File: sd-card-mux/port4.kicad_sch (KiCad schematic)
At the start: 10 parts, among them J201 47309-2285, U201 74LVC1G3157, U202 74LVC1G3157, U203 74LVC1G3157, U204 74LVC1G3157, U205 74LVC1G3157, U206 74LVC1G3157

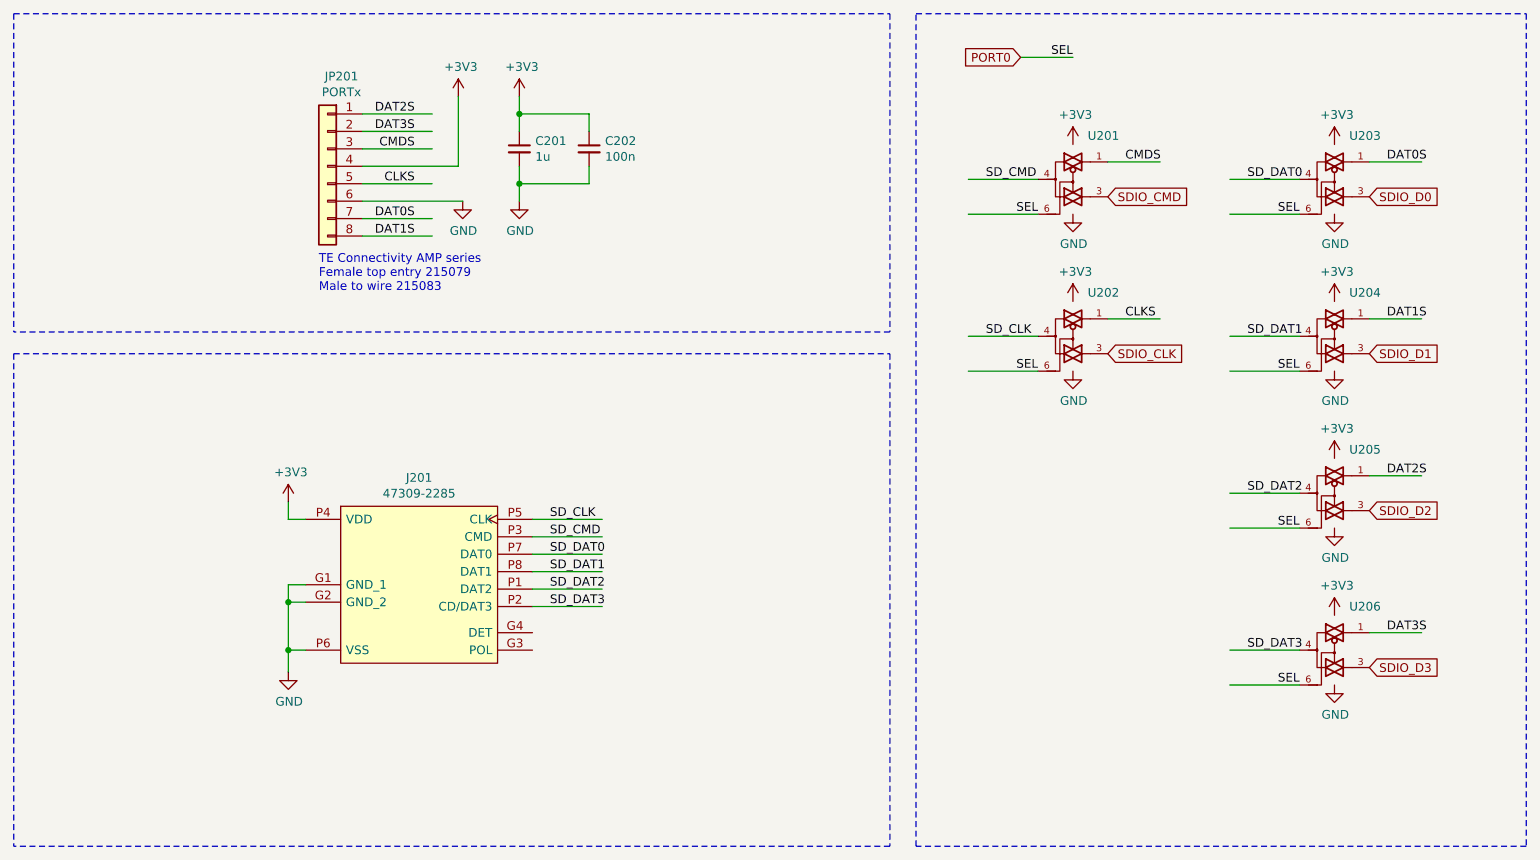
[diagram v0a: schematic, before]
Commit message: Added MCP23008 alternative
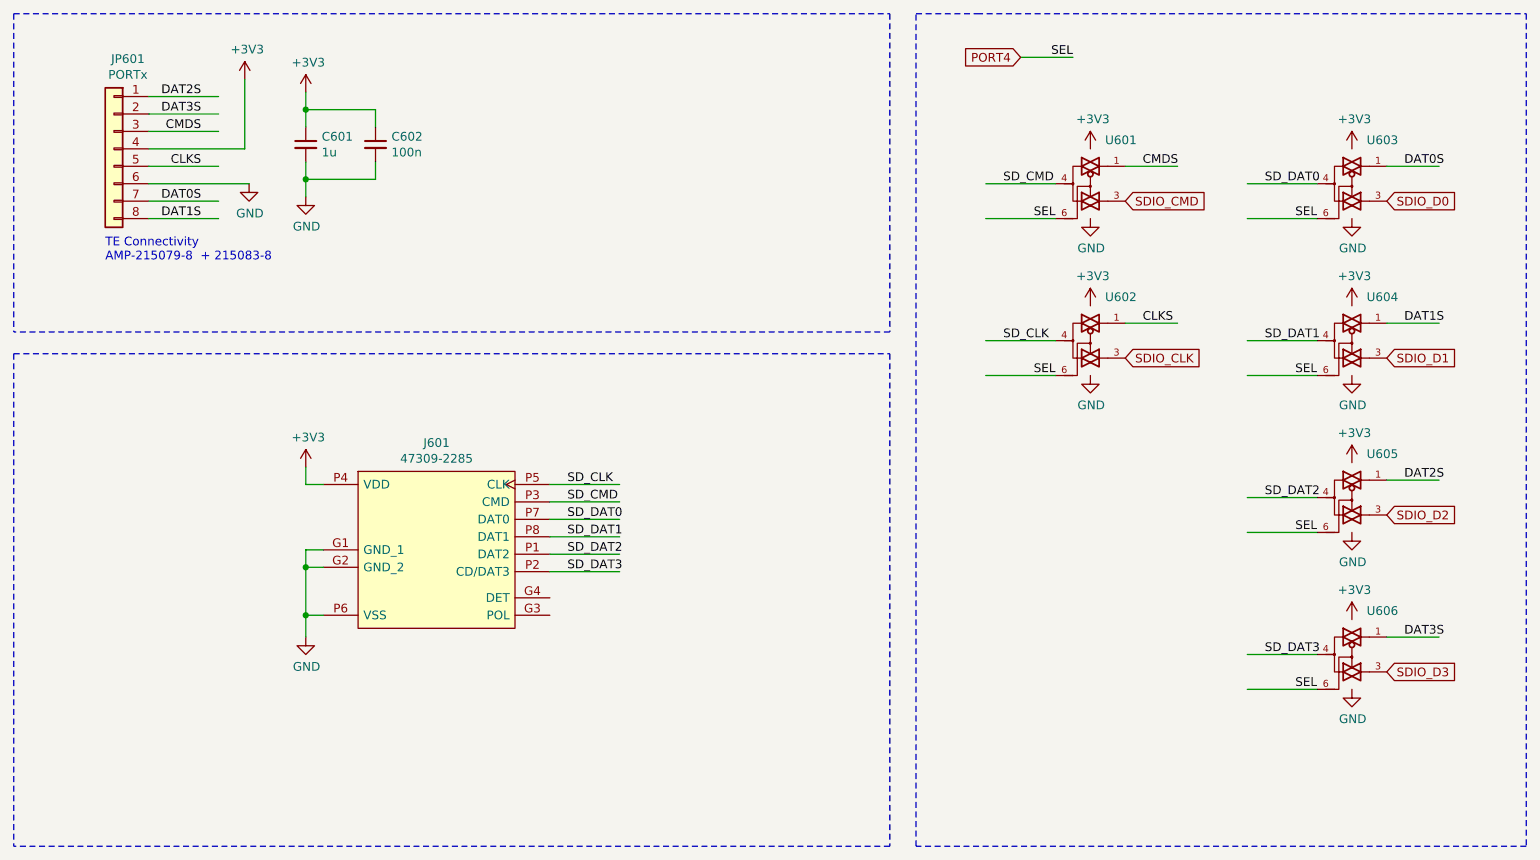
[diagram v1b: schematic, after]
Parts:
- removed C201: 1u, Capacitor_SMD:C_0402_1005Metric, symbol Device:C_Small
- removed C202: 100n, Capacitor_SMD:C_0402_1005Metric, symbol Device:C_Small
- removed J201: 47309-2285, footprints:47309-2285, symbol 47309-2285:47309-2285
- removed JP201: PORTx, Connector_JST:JST_PH_S8B-PH-K_1x08_P2.00mm_Horizontal, symbol Connector_Generic:Conn_01x08
- removed U201, U202, U203, U204, U205, U206: 74LVC1G3157, Package_TO_SOT_SMD:SOT-363_SC-70-6, symbol 74LVC1G3157:74LVC1G3157
- added C601: 1u, Capacitor_SMD:C_0402_1005Metric, symbol Device:C_Small
- added C602: 100n, Capacitor_SMD:C_0402_1005Metric, symbol Device:C_Small
- added J601: 47309-2285, footprints:47309-2285, symbol 47309-2285:47309-2285
- added JP601: PORTx, Connector_JST:JST_PH_S8B-PH-K_1x08_P2.00mm_Horizontal, symbol Connector_Generic:Conn_01x08
- added U601, U602, U603, U604, U605, U606: 74LVC1G3157, Package_TO_SOT_SMD:SOT-363_SC-70-6, symbol 74LVC1G3157:74LVC1G3157
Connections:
- net +3V3: now also C601.1, C602.1, J601.P4 (VDD), JP601.4 (Pin_4), U601.5 (VCC), U602.5 (VCC), U603.5 (VCC), U604.5 (VCC), U605.5 (VCC), U606.5 (VCC)
- net CLKS: now also JP601.5 (Pin_5), U602.1
- net CMDS: now also JP601.3 (Pin_3), U601.1
- net DAT0S: now also JP601.7 (Pin_7), U603.1
- net DAT1S: now also JP601.8 (Pin_8), U604.1
- net DAT2S: now also JP601.1 (Pin_1), U605.1
- net DAT3S: now also JP601.2 (Pin_2), U606.1
- net GND: now also C601.2, C602.2, J601.G1 (GND_1), J601.G2 (GND_2), J601.P6 (VSS), JP601.6 (Pin_6), U601.2 (GND), U602.2 (GND), U603.2 (GND), U604.2 (GND), U605.2 (GND), U606.2 (GND)
- net SDIO_CLK: now also U602.3
- net SDIO_CMD: now also U601.3
- net SDIO_D0: now also U603.3
- net SDIO_D1: now also U604.3
- net SDIO_D2: now also U605.3
- net SDIO_D3: now also U606.3
- net SD_CLK: now also J601.P5 (CLK), U602.4
- net SD_CMD: now also J601.P3 (CMD), U601.4
- net SD_DAT0: now also J601.P7 (DAT0), U603.4
- net SD_DAT1: now also J601.P8 (DAT1), U604.4
- net SD_DAT2: now also J601.P1 (DAT2), U605.4
- net SD_DAT3: now also J601.P2 (CD/DAT3), U606.4
- new net PORT4: U601.6, U602.6, U603.6, U604.6, U605.6, U606.6
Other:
- note added: "TE Connectivity AMP-215079-8 + 215083-8"
- note removed: "TE Connectivity AMP series Female top entry 215079 Male to wire 215083"

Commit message: Addedd missing upload port
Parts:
- C601: LCSC Part# (none) -> C52923
- C602: LCSC Part# (none) -> C1525
- JP601: footprint Connector_JST:JST_PH_S8B-PH-K_1x08_P2.00mm_Horizontal -> footprints:ConnectorMicromatch-8
- U601, U602, U603, U604, U605, U606: LCSC Part# (none) -> C38663
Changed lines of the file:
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@@
+      (effects (font (size 1.27 1.27)) hide)
+    )
+    (property "LCSC Part#" "C52923" (id 4) (at 63.5 38.1 0)
       (effects (font (size 1.27 1.27)) hide)
     )
@@
       (effects (font (size 1.27 1.27)) hide)
     )
+    (property "LCSC Part#" "C1525" (id 4) (at 73.66 38.1 0)
+      (effects (font (size 1.27 1.27)) hide)
+    )
   )
   (symbol (lib_name "74LVC1G3157:74LVC1G3157_2") (lib_id "74LVC1G3157:74LVC1G3157") (at 177.8 43.815 0) (unit 1)
@@
     )
     (property "Datasheet" "https://www.ti.com/lit/ds/symlink/sn74lvc1g3157.pdf" (id 3) (at 177.8 43.815 0)
+      (effects (font (size 1.27 1.27)) hide)
+    )
+    (property "LCSC Part#" " C38663" (id 4) (at 177.8 43.815 0)
       (effects (font (size 1.27 1.27)) hide)
     )
@@
       (effects (font (size 1.27 1.27)) hide)
     )
+    (property "LCSC Part#" " C38663" (id 4) (at 177.8 66.675 0)
+      (effects (font (size 1.27 1.27)) hide)
+    )
   )
   (symbol (lib_id "74LVC1G3157:74LVC1G3157") (at 215.9 43.815 0) (unit 1)
@@
     )
     (property "Datasheet" "https://www.ti.com/lit/ds/symlink/sn74lvc1g3157.pdf" (id 3) (at 215.9 43.815 0)
+      (effects (font (size 1.27 1.27)) hide)
+    )
+    (property "LCSC Part#" " C38663" (id 4) (at 215.9 43.815 0)
       (effects (font (size 1.27 1.27)) hide)
     )
@@
       (effects (font (size 1.27 1.27)) hide)
     )
+    (property "LCSC Part#" " C38663" (id 4) (at 215.9 66.675 0)
+      (effects (font (size 1.27 1.27)) hide)
+    )
   )
   (symbol (lib_id "74LVC1G3157:74LVC1G3157") (at 215.9 89.535 0) (unit 1)
@@
     )
     (property "Datasheet" "https://www.ti.com/lit/ds/symlink/sn74lvc1g3157.pdf" (id 3) (at 215.9 89.535 0)
+      (effects (font (size 1.27 1.27)) hide)
+    )
+    (property "LCSC Part#" " C38663" (id 4) (at 215.9 89.535 0)
       (effects (font (size 1.27 1.27)) hide)
     )
@@
       (effects (font (size 1.27 1.27)) hide)
     )
+    (property "LCSC Part#" " C38663" (id 4) (at 215.9 112.395 0)
+      (effects (font (size 1.27 1.27)) hide)
+    )
   )
   (symbol (lib_id "Connector_Generic:Conn_01x08") (at 35.56 38.735 0) (mirror y) (unit 1)
@@
     (property "Reference" "JP601" (id 0) (at 37.592 25.635 0))
     (property "Value" "PORTx" (id 1) (at 37.592 27.9335 0))
-    (property "Footprint" "Connector_JST:JST_PH_S8B-PH-K_1x08_P2.00mm_Horizontal" (id 2) (at 35.56 38.735 0)
+    (property "Footprint" "footprints:ConnectorMicromatch-8" (id 2) (at 35.56 38.735 0)
       (effects (font (size 1.27 1.27)) hide)
     )

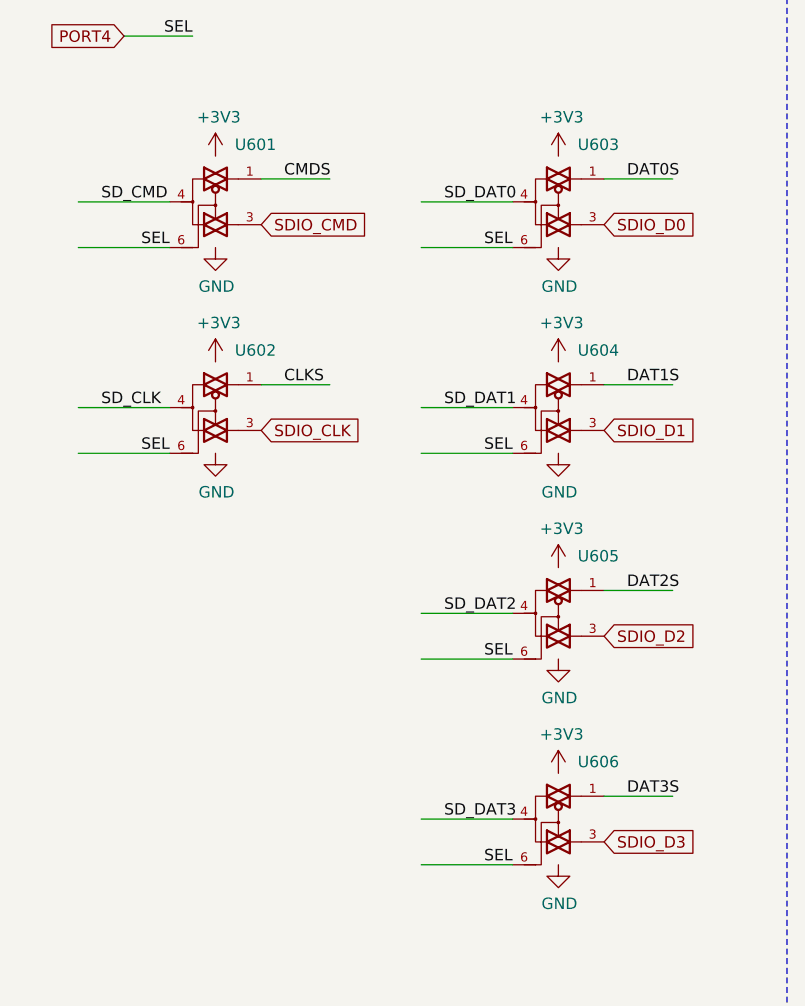
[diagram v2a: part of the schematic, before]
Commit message: Correction of inverted pins
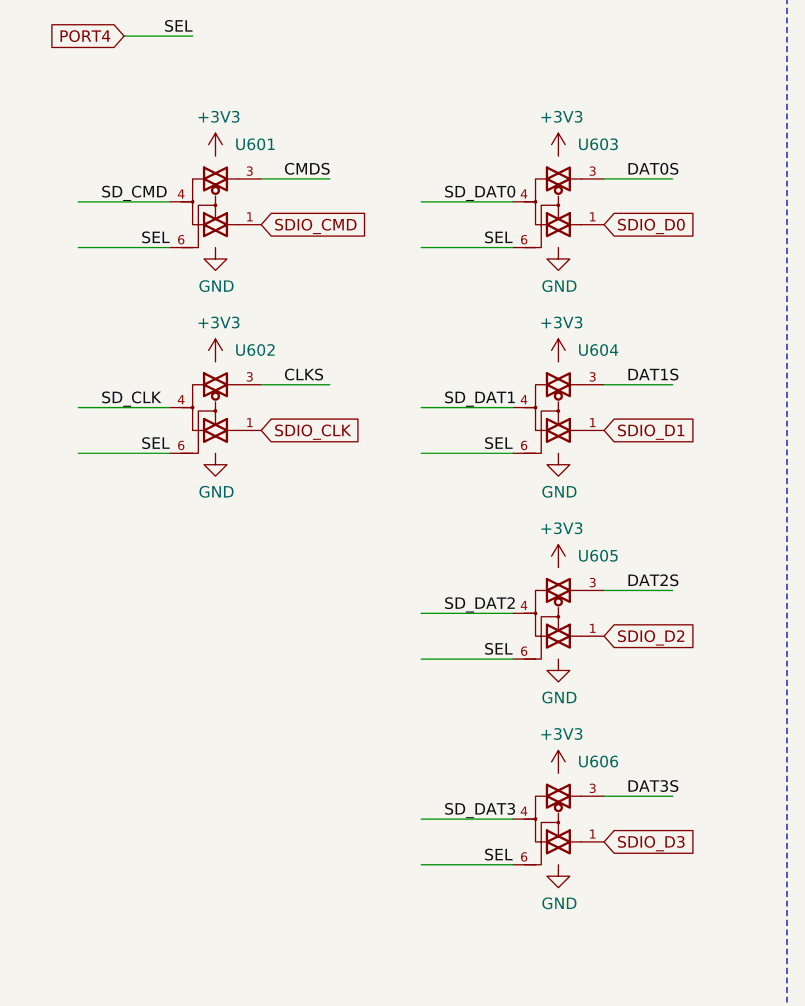
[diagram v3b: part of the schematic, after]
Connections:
- net CLKS: now also U602.3; no longer U602.1
- net CMDS: now also U601.3; no longer U601.1
- net DAT0S: now also U603.3; no longer U603.1
- net DAT1S: now also U604.3; no longer U604.1
- net DAT2S: now also U605.3; no longer U605.1
- net DAT3S: now also U606.3; no longer U606.1
- net SDIO_CLK: now also U602.1; no longer U602.3
- net SDIO_CMD: now also U601.1; no longer U601.3
- net SDIO_D0: now also U603.1; no longer U603.3
- net SDIO_D1: now also U604.1; no longer U604.3
- net SDIO_D2: now also U605.1; no longer U605.3
- net SDIO_D3: now also U606.1; no longer U606.3
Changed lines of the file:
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@@
 (kicad_sch (version 20200608) (host eeschema "(5.99.0-1973-g8c57821e9)")
-  (page 1 9)
+  (page 6 9)
   (paper "A4")
   (junction (at 63.5 33.02))
@@
     )
   )
-  (symbol (lib_id "74LVC1G3157:74LVC1G3157") (at 177.8 66.675 0) (unit 1)
+  (symbol (lib_name "74LVC1G3157:74LVC1G3157_1") (lib_id "74LVC1G3157:74LVC1G3157") (at 177.8 66.675 0) (unit 1)
     (in_bom yes) (on_board yes)
     (property "Reference" "U602" (id 0) (at 182.245 60.325 0))
@@
     )
   )
-  (symbol (lib_id "74LVC1G3157:74LVC1G3157") (at 215.9 43.815 0) (unit 1)
+  (symbol (lib_name "74LVC1G3157:74LVC1G3157_3") (lib_id "74LVC1G3157:74LVC1G3157") (at 215.9 43.815 0) (unit 1)
     (in_bom yes) (on_board yes)
     (property "Reference" "U603" (id 0) (at 220.345 37.465 0))
@@
     )
   )
-  (symbol (lib_id "74LVC1G3157:74LVC1G3157") (at 215.9 66.675 0) (unit 1)
+  (symbol (lib_name "74LVC1G3157:74LVC1G3157_4") (lib_id "74LVC1G3157:74LVC1G3157") (at 215.9 66.675 0) (unit 1)
     (in_bom yes) (on_board yes)
     (property "Reference" "U604" (id 0) (at 220.345 60.325 0))
@@
     )
   )
-  (symbol (lib_id "74LVC1G3157:74LVC1G3157") (at 215.9 89.535 0) (unit 1)
+  (symbol (lib_name "74LVC1G3157:74LVC1G3157_5") (lib_id "74LVC1G3157:74LVC1G3157") (at 215.9 89.535 0) (unit 1)
     (in_bom yes) (on_board yes)
     (property "Reference" "U605" (id 0) (at 220.345 83.185 0))

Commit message: Removal of host port and preparation for manufacturing
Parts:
- J601: Mechanical (none) -> T
- JP601: Mechanical (none) -> T; TME Part# (none) -> MM2x5
- U601, U602, U603, U604, U605, U606: LCSC Part# C38663 -> C265126; Rotation (none) -> 0
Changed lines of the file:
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@@
       (effects (font (size 1.27 1.27)) hide)
     )
-    (property "LCSC Part#" " C38663" (id 4) (at 177.8 43.815 0)
+    (property "LCSC Part#" "C265126" (id 4) (at 177.8 43.815 0)
+      (effects (font (size 1.27 1.27)) hide)
+    )
+    (property "Rotation" "0" (id 4) (at 177.8 43.815 0)
       (effects (font (size 1.27 1.27)) hide)
     )
@@
       (effects (font (size 1.27 1.27)) hide)
     )
-    (property "LCSC Part#" " C38663" (id 4) (at 177.8 66.675 0)
+    (property "LCSC Part#" "C265126" (id 4) (at 177.8 66.675 0)
+      (effects (font (size 1.27 1.27)) hide)
+    )
+    (property "Rotation" "0" (id 4) (at 177.8 66.675 0)
       (effects (font (size 1.27 1.27)) hide)
     )
@@
       (effects (font (size 1.27 1.27)) hide)
     )
-    (property "LCSC Part#" " C38663" (id 4) (at 215.9 43.815 0)
+    (property "LCSC Part#" "C265126" (id 4) (at 215.9 43.815 0)
+      (effects (font (size 1.27 1.27)) hide)
+    )
+    (property "Rotation" "0" (id 4) (at 215.9 43.815 0)
       (effects (font (size 1.27 1.27)) hide)
     )
@@
       (effects (font (size 1.27 1.27)) hide)
     )
-    (property "LCSC Part#" " C38663" (id 4) (at 215.9 66.675 0)
+    (property "LCSC Part#" "C265126" (id 4) (at 215.9 66.675 0)
+      (effects (font (size 1.27 1.27)) hide)
+    )
+    (property "Rotation" "0" (id 4) (at 215.9 66.675 0)
       (effects (font (size 1.27 1.27)) hide)
     )
@@
       (effects (font (size 1.27 1.27)) hide)
     )
-    (property "LCSC Part#" " C38663" (id 4) (at 215.9 89.535 0)
+    (property "LCSC Part#" "C265126" (id 4) (at 215.9 89.535 0)
+      (effects (font (size 1.27 1.27)) hide)
+    )
+    (property "Rotation" "0" (id 4) (at 215.9 89.535 0)
       (effects (font (size 1.27 1.27)) hide)
     )
@@
       (effects (font (size 1.27 1.27)) hide)
     )
-    (property "LCSC Part#" " C38663" (id 4) (at 215.9 112.395 0)
+    (property "LCSC Part#" "C265126" (id 4) (at 215.9 112.395 0)
+      (effects (font (size 1.27 1.27)) hide)
+    )
+    (property "Rotation" "0" (id 4) (at 215.9 112.395 0)
       (effects (font (size 1.27 1.27)) hide)
     )
@@
     )
     (property "Datasheet" "~" (id 3) (at 35.56 38.735 0)
+      (effects (font (size 1.27 1.27)) hide)
+    )
+    (property "TME Part#" "MM2x5" (id 4) (at 35.56 38.735 0)
+      (effects (font (size 1.27 1.27)) hide)
+    )
+    (property "Mechanical" "T" (id 4) (at 35.56 38.735 0)
       (effects (font (size 1.27 1.27)) hide)
     )
@@
       (effects (font (size 1.27 1.27)) (justify left) hide)
     )
+    (property "Mechanical" "T" (id 4) (at 66.04 88.265 0)
+      (effects (font (size 1.27 1.27)) hide)
+    )
   )
